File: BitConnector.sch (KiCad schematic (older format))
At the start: 23 parts, among them J1 JTAG, J2 Conn_01x02, SW1 reset, U1 XC95##XL-VQ44, U2 74LVC2G14

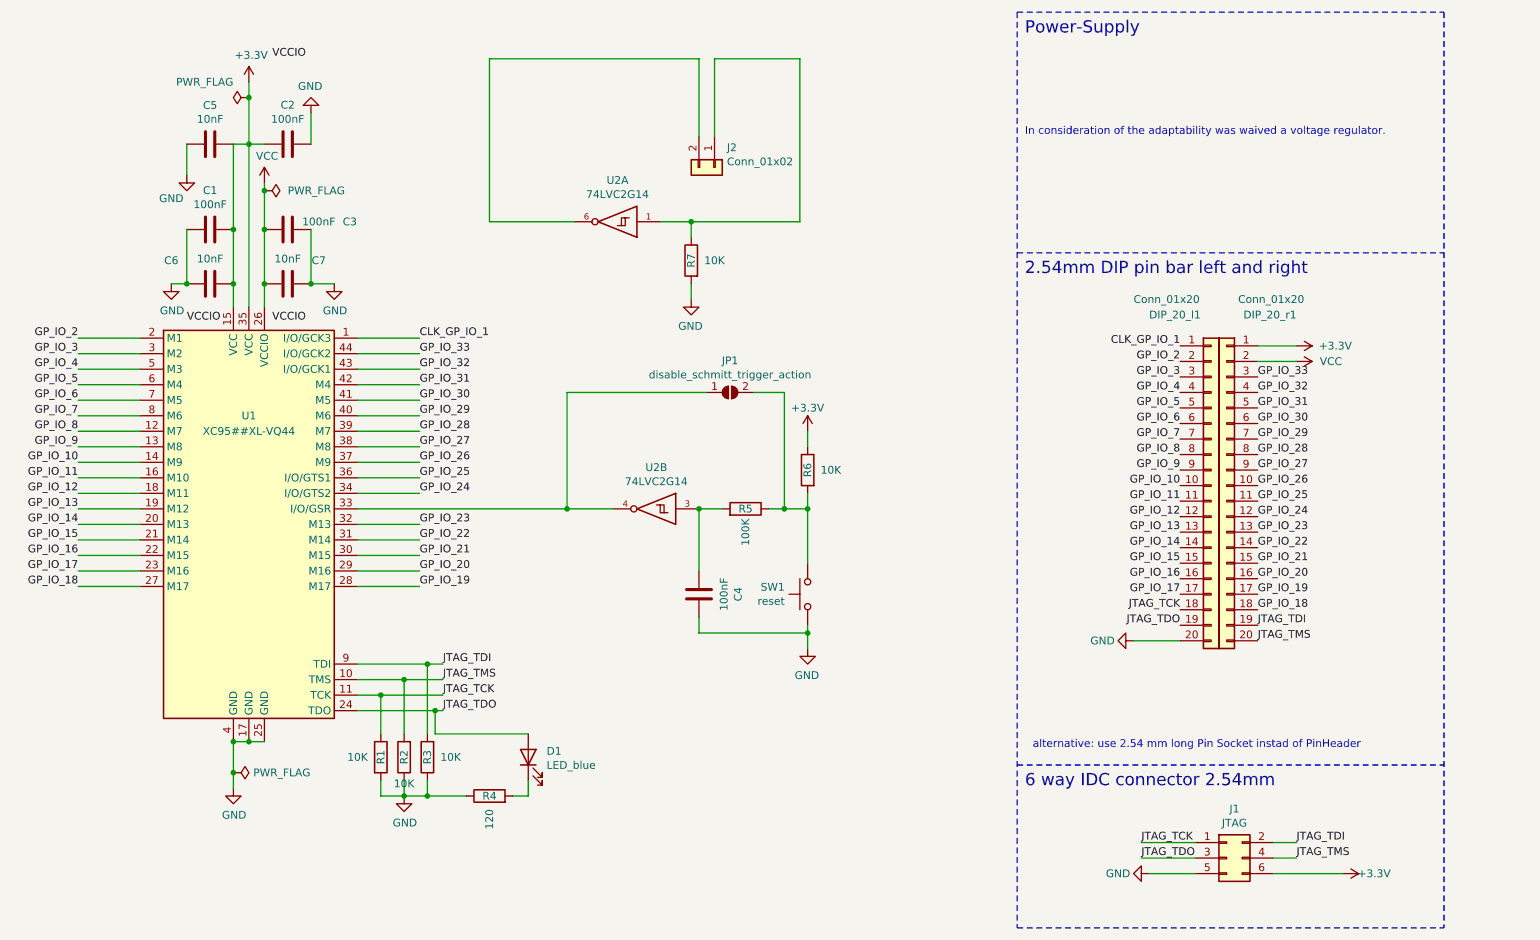
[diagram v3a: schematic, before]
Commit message: Revise the concept of PCB labeling
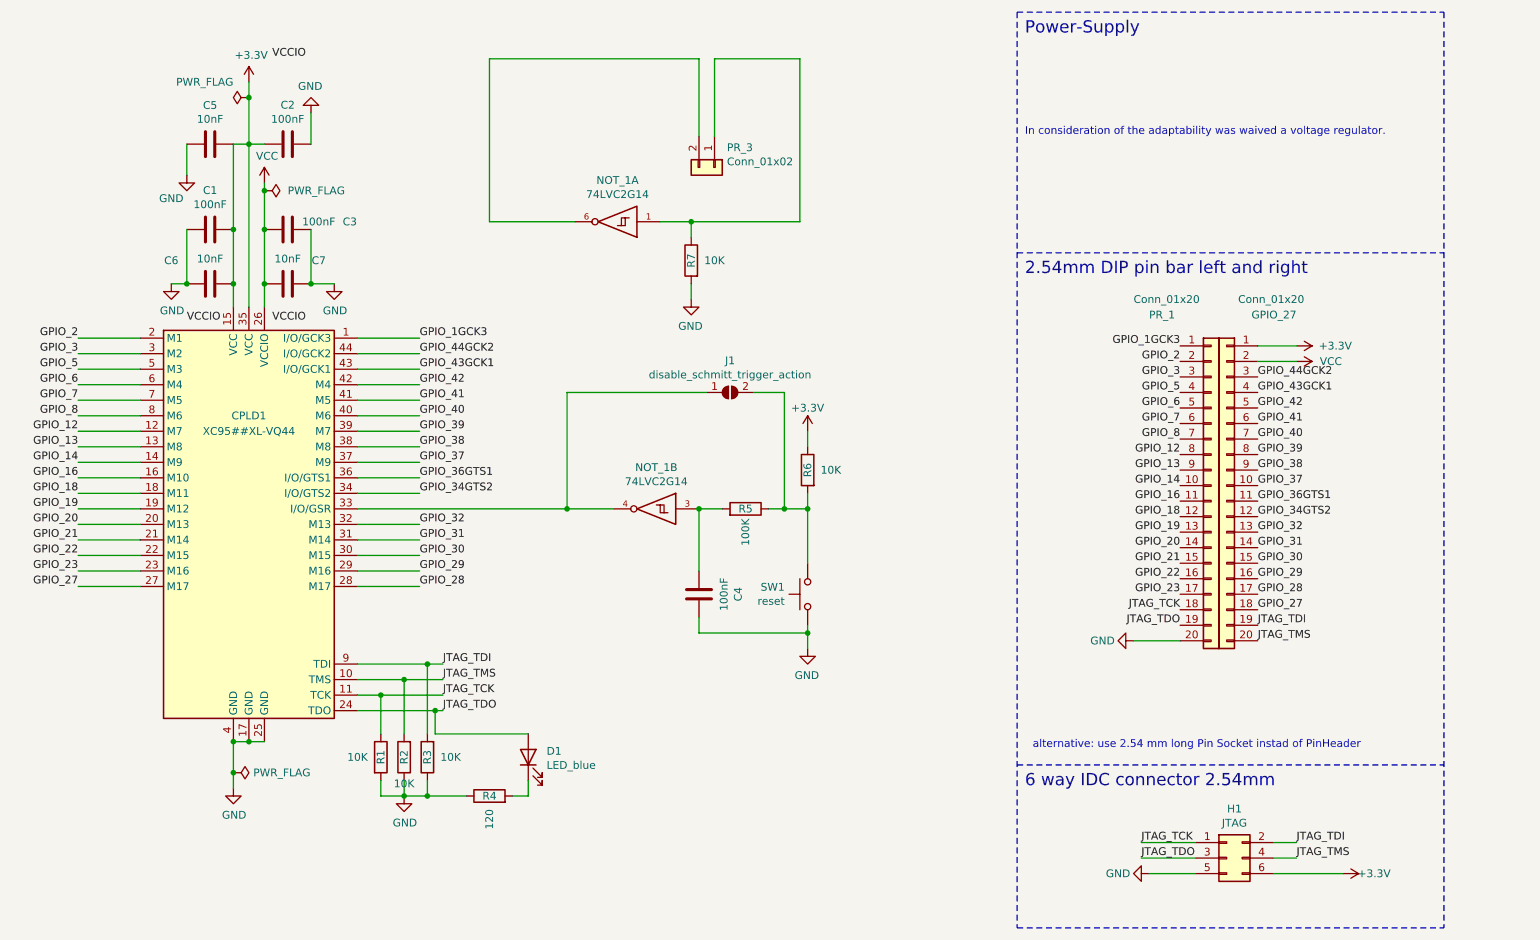
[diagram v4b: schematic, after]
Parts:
- renumbered U1 to CPLD1, DIP_20_r1 to GPIO_27, J1 to H1, JP1 to J1, U2 to NOT_1, DIP_20_l1 to PR_1, J2 to PR_3
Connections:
- net CLK_GP_IO_1 renamed GPIO_1GCK3
- net GP_IO_10 renamed GPIO_14
- net GP_IO_11 renamed GPIO_16
- net GP_IO_12 renamed GPIO_18
- net GP_IO_13 renamed GPIO_19
- net GP_IO_14 renamed GPIO_20
- net GP_IO_15 renamed GPIO_21
- net GP_IO_16 renamed GPIO_22
- net GP_IO_17 renamed GPIO_23
- net GP_IO_18 renamed GPIO_27
- net GP_IO_19 renamed GPIO_28
- net GP_IO_2 renamed GPIO_2
- net GP_IO_20 renamed GPIO_29
- net GP_IO_21 renamed GPIO_30
- net GP_IO_22 renamed GPIO_31
- net GP_IO_23 renamed GPIO_32
- net GP_IO_24 renamed GPIO_34GTS2
- net GP_IO_25 renamed GPIO_36GTS1
- net GP_IO_26 renamed GPIO_37
- net GP_IO_27 renamed GPIO_38
- net GP_IO_28 renamed GPIO_39
- net GP_IO_29 renamed GPIO_40
- net GP_IO_3 renamed GPIO_3
- net GP_IO_30 renamed GPIO_41
- net GP_IO_31 renamed GPIO_42
- net GP_IO_32 renamed GPIO_43GCK1
- net GP_IO_33 renamed GPIO_44GCK2
- net GP_IO_4 renamed GPIO_5
- net GP_IO_5 renamed GPIO_6
- net GP_IO_6 renamed GPIO_7
- net GP_IO_7 renamed GPIO_8
- net GP_IO_8 renamed GPIO_12
- net GP_IO_9 renamed GPIO_13
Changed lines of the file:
@@
 Sheet 1 1
 Title "XC95## VQ44 to DIP 40"
-Date "2021-02-01"
-Rev "v04X"
+Date "2021-06-23"
+Rev "v05Xe"
 Comp ""
 Comment1 ""
@@
 	4600 5200 4600 4750
 Text Label 9950 3800 0    50   ~ 0
-GP_IO_24
+GPIO_34GTS2
 Text Label 9950 3700 0    50   ~ 0
-GP_IO_25
+GPIO_36GTS1
 Text Label 9950 3600 0    50   ~ 0
-GP_IO_26
+GPIO_37
 Text Label 9950 3500 0    50   ~ 0
-GP_IO_27
+GPIO_38
 Text Label 9950 3400 0    50   ~ 0
-GP_IO_28
+GPIO_39
 Text Label 9950 3300 0    50   ~ 0
-GP_IO_29
+GPIO_40
 Text Label 9950 3200 0    50   ~ 0
-GP_IO_30
+GPIO_41
 Text Label 9950 3100 0    50   ~ 0
-GP_IO_31
+GPIO_42
 Text Label 9950 3000 0    50   ~ 0
-GP_IO_32
+GPIO_43GCK1
 Wire Notes Line width 20 style solid
 	8400 2100 11150 2100
@@
 2.54mm DIP pin bar left and right
 $Comp
-L Connector_Generic:Conn_01x20 DIP_20_l1
+L Connector_Generic:Conn_01x20 PR_1
 U 1 1 5C39D223
 P 9650 3600
-F 0 "DIP_20_l1" H 9250 4700 50  0000 L CNN
+F 0 "PR_1" H 9250 4700 50  0000 L CNN
 F 1 "Conn_01x20" H 9150 4800 50  0000 L CNN
 F 2 "Connector_PinHeader_2.54mm:PinHeader_1x20_P2.54mm_Vertical" H 9650 3600 50  0001 C CNN
@@
 $EndComp
 $Comp
-L Connector_Generic:Conn_01x20 DIP_20_r1
+L Connector_Generic:Conn_01x20 GPIO_27
 U 1 1 5C39F10C
 P 9750 3600
-F 0 "DIP_20_r1" H 9300 4700 50  0000 L CNN
+F 0 "GPIO_27" H 9300 4700 50  0000 L CNN
 F 1 "Conn_01x20" H 9250 4800 50  0000 L CNN
 F 2 "Connector_PinHeader_2.54mm:PinHeader_1x20_P2.54mm_Vertical" H 9750 3600 50  0001 C CNN
@@
 $EndComp
 Text Label 4550 2950 0    50   ~ 0
-GP_IO_31
+GPIO_42
 Text Label 4550 2850 0    50   ~ 0
-GP_IO_32
+GPIO_43GCK1
 Text Label 4550 2750 0    50   ~ 0
-GP_IO_33
+GPIO_44GCK2
 Text Label 2350 3150 2    50   ~ 0
-GP_IO_7
+GPIO_8
 Text Label 2350 2650 2    50   ~ 0
-GP_IO_2
+GPIO_2
 Text Label 2350 2750 2    50   ~ 0
-GP_IO_3
+GPIO_3
 Text Label 2350 2950 2    50   ~ 0
-GP_IO_5
+GPIO_6
 Text Label 2350 2850 2    50   ~ 0
-GP_IO_4
+GPIO_5
 Text Label 2350 3250 2    50   ~ 0
-GP_IO_8
+GPIO_12
 Text Label 2350 3050 2    50   ~ 0
-GP_IO_6
+GPIO_7
 Text Label 2350 3350 2    50   ~ 0
-GP_IO_9
+GPIO_13
 Text Label 2350 3450 2    50   ~ 0
-GP_IO_10
+GPIO_14
 Text Label 2350 3550 2    50   ~ 0
-GP_IO_11
+GPIO_16
 Text Label 2350 3650 2    50   ~ 0
-GP_IO_12
-Text Label 2350 3750 2    50   ~ 0
-GP_IO_13
+GPIO_18
 Text Label 2350 3850 2    50   ~ 0
-GP_IO_14
+GPIO_20
 Text Label 2350 3950 2    50   ~ 0
-GP_IO_15
+GPIO_21
 Text Label 9450 3600 2    50   ~ 0
-GP_IO_10
+GPIO_14
 Text Label 9450 2800 2    50   ~ 0
-GP_IO_2
+GPIO_2
 Text Label 9450 2900 2    50   ~ 0
-GP_IO_3
+GPIO_3
 Text Label 9450 3000 2    50   ~ 0
-GP_IO_4
+GPIO_5
 Text Label 9450 3100 2    50   ~ 0
-GP_IO_5
+GPIO_6
 Text Label 9450 3200 2    50   ~ 0
-GP_IO_6
+GPIO_7
 Text Label 9450 3300 2    50   ~ 0
-GP_IO_7
+GPIO_8
 Text Label 9450 3400 2    50   ~ 0
-GP_IO_8
+GPIO_12
 Text Label 9450 3800 2    50   ~ 0
-GP_IO_12
+GPIO_18
 Text Label 9450 3900 2    50   ~ 0
-GP_IO_13
+GPIO_19
 Text Label 9450 4000 2    50   ~ 0
-GP_IO_14
+GPIO_20
 Text Label 9450 4100 2    50   ~ 0
-GP_IO_15
+GPIO_21
 Text Label 9450 4200 2    50   ~ 0
-GP_IO_16
+GPIO_22
 Wire Wire Line
 	9450 4600 9150 4600
 Text Label 9450 4300 2    50   ~ 0
-GP_IO_17
+GPIO_23
 Text Label 9950 4400 0    50   ~ 0
-GP_IO_18
-Text Label 9450 2700 2    50   ~ 0
-CLK_GP_IO_1
+GPIO_27
 Text Label 9950 4300 0    50   ~ 0
-GP_IO_19
+GPIO_28
 Text Label 9950 4200 0    50   ~ 0
-GP_IO_20
+GPIO_29
 Text Label 9950 4100 0    50   ~ 0
-GP_IO_21
+GPIO_30
 Text Label 4550 4250 0    50   ~ 0
-GP_IO_19
+GPIO_28
 Text Label 9950 3900 0    50   ~ 0
-GP_IO_23
+GPIO_32
 Text Label 2350 4050 2    50   ~ 0
-GP_IO_16
+GPIO_22
 Text Label 2350 4150 2    50   ~ 0
-GP_IO_17
+GPIO_23
 Text Label 2350 4250 2    50   ~ 0
-GP_IO_18
+GPIO_27
 Text Label 9950 4000 0    50   ~ 0
-GP_IO_22
+GPIO_31
 Text Label 4550 4150 0    50   ~ 0
-GP_IO_20
+GPIO_29
 Text Label 4550 4050 0    50   ~ 0
-GP_IO_21
+GPIO_30
 Text Label 4550 3950 0    50   ~ 0
-GP_IO_22
+GPIO_31
 Text Label 4550 3850 0    50   ~ 0
-GP_IO_23
+GPIO_32
 Text Label 4550 3650 0    50   ~ 0
-GP_IO_24
+GPIO_34GTS2
 Text Label 4550 3550 0    50   ~ 0
-GP_IO_25
+GPIO_36GTS1
 Text Label 4550 3450 0    50   ~ 0
-GP_IO_26
+GPIO_37
 Text Label 4550 3350 0    50   ~ 0
-GP_IO_27
+GPIO_38
 Text Label 4550 3250 0    50   ~ 0
-GP_IO_28
+GPIO_39
 Text Label 9450 3500 2    50   ~ 0
-GP_IO_9
+GPIO_13
 Text Label 9450 3700 2    50   ~ 0
-GP_IO_11
+GPIO_16
 Text Label 9950 4500 0    50   ~ 0
 JTAG_TDI
@@
 JTAG_TDO
 Text Label 4550 2650 0    50   ~ 0
-CLK_GP_IO_1
+GPIO_1GCK3
 Text Label 4550 3150 0    50   ~ 0
-GP_IO_29
+GPIO_40
 Wire Wire Line
 	2350 3150 2750 3150
 Text Label 4550 3050 0    50   ~ 0
-GP_IO_30
+GPIO_41
 Wire Wire Line
 	4150 3050 4550 3050
 Text Label 9950 2900 0    50   ~ 0
-GP_IO_33
-$Comp
-L XC96xxxl:Xilinx_CPLD_VQFP_2_DIP-rescue_XC9536XL-VQ44-Xilinx-VQ44-Xilinx_CPLD_VQFP_2_DIP-rescue-BitConnector-BitConnector-rescue-BitConnector-rescue U1
+GPIO_44GCK2
+$Comp
+L XC96xxxl:Xilinx_CPLD_VQFP_2_DIP-rescue_XC9536XL-VQ44-Xilinx-VQ44-Xilinx_CPLD_VQFP_2_DIP-rescue-BitConnector-BitConnector-rescue-BitConnector-rescue CPLD1
 U 1 1 5C7597D2
 P 3450 3850
-F 0 "U1" H 3450 4550 50  0000 C CNN
+F 0 "CPLD1" H 3450 4550 50  0000 C CNN
 F 1 "XC95##XL-VQ44" H 3450 4450 50  0000 C CNN
 F 2 "Package_QFP:LQFP-44_10x10mm_P0.8mm" H 3450 3850 50  0001 C CNN
@@
 In consideration of the adaptability was waived a voltage regulator.
 $Comp
-L Connector_Generic:Conn_02x03_Odd_Even J1
+L Connector_Generic:Conn_02x03_Odd_Even H1
 U 1 1 5D841E29
 P 9750 6000
-F 0 "J1" H 9800 6317 50  0000 C CNN
+F 0 "H1" H 9800 6317 50  0000 C CNN
 F 1 "JTAG" H 9800 6226 50  0000 C CNN
 F 2 "Connector_IDC:IDC-Header_2x03_P2.54mm_Vertical" H 9750 6000 50  0001 C CNN
@@
 	5000 1900 5000 850
 $Comp
-L Connector_Generic:Conn_01x02 J2
+L Connector_Generic:Conn_01x02 PR_3
 U 1 1 5DC15FDD
 P 6450 1550
-F 0 "J2" V 6322 1630 50  0000 L CNN
+F 0 "PR_3" V 6322 1630 50  0000 L CNN
 F 1 "Conn_01x02" V 6413 1630 50  0000 L CNN
 F 2 "Connector_PinSocket_2.54mm:PinSocket_1x02_P2.54mm_Vertical" H 6450 1550 50  0001 C CNN
@@
 $EndComp
 $Comp
-L 74xGxx:74LVC2G14 U2
+L 74xGxx:74LVC2G14 NOT_1
 U 1 1 5DBBF222
 P 5800 1900
-F 0 "U2" H 5775 1633 50  0000 C CNN
+F 0 "NOT_1" H 5775 1633 50  0000 C CNN
 F 1 "74LVC2G14" H 5775 1724 50  0000 C CNN
 F 2 "Package_SO:SC-74-6_1.5x2.9mm_P0.95mm" H 5800 1900 50  0001 C CNN
@@
 $EndComp
 $Comp
-L 74xGxx:74LVC2G14 U2
+L 74xGxx:74LVC2G14 NOT_1
 U 2 1 5DB3A7BA
 P 6050 3750
-F 0 "U2" H 6025 4017 50  0000 C CNN
+F 0 "NOT_1" H 6025 4017 50  0000 C CNN
 F 1 "74LVC2G14" H 6025 3926 50  0000 C CNN
 F 2 "Package_SO:SC-74-6_1.5x2.9mm_P0.95mm" H 6050 3750 50  0001 C CNN
@@
 	6350 4550 7050 4550
 $Comp
-L Jumper:SolderJumper_2_Open JP1
+L Jumper:SolderJumper_2_Open J1
 U 1 1 5DB867A4
 P 6550 3000
-F 0 "JP1" H 6550 3205 50  0000 C CNN
+F 0 "J1" H 6550 3205 50  0000 C CNN
 F 1 "disable_schmitt_trigger_action" H 6550 3114 50  0000 C CNN
 F 2 "Jumper:SolderJumper-2_P1.3mm_Open_RoundedPad1.0x1.5mm" H 6550 3000 50  0001 C CNN
@@
 Wire Wire Line
 	3350 2300 3350 2450
+Text Label 9450 2700 2    50   ~ 0
+GPIO_1GCK3
+Text Label 2350 3750 2    50   ~ 0
+GPIO_19
 $EndSCHEMATC
